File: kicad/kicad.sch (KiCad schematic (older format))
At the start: 46 parts, among them J1 Power, J2 Address In, J3 Counter Reset Value, J4 5V, J5 Mode In, J6 GND, J7 VGA Out, J8 L77HDE15SD1CH4F, J9 Data In, U1 74LS157, U10 SN74LS682N, U11 74LS161, U12 74LS157, U13 74LS157, U14 74LS161, U15 74LS157, U16 74LS157, U17 74LS161, U18 SN74HC32N, U19 74LS161, U2 74LS157, U20 SN74LS04N, U21 AS6C4008-55PCN, U22 SN74LS74AN, U23 AS6C4008-55PCN, U24 SN74LS244N, U25 SN74LS244N, U26 SN74LS244N, U27 SN74LS244N, U3 SN74LS74AN, U4 SN74LS682N, U5 74LS157, U6 74LS157, U7 74LS161, U8 74LS157, U9 74LS157, X1 CXO_DIP8

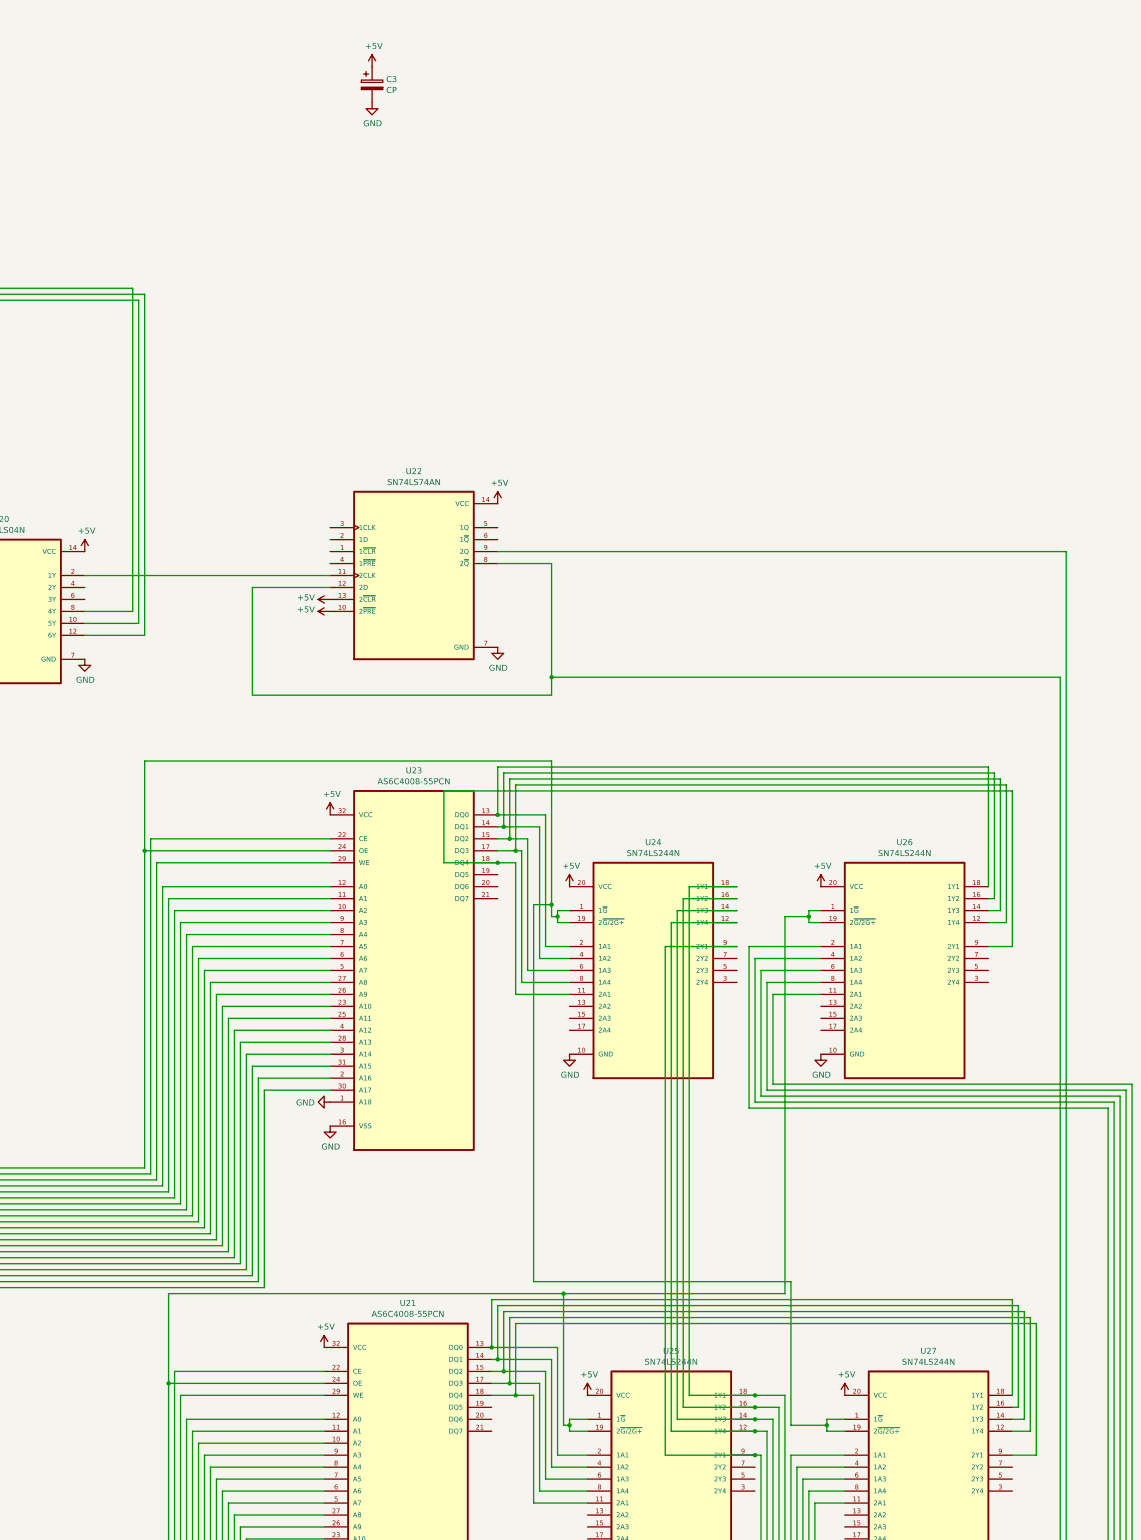
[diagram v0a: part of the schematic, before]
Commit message: Update schematic to account for SRAM enable time.
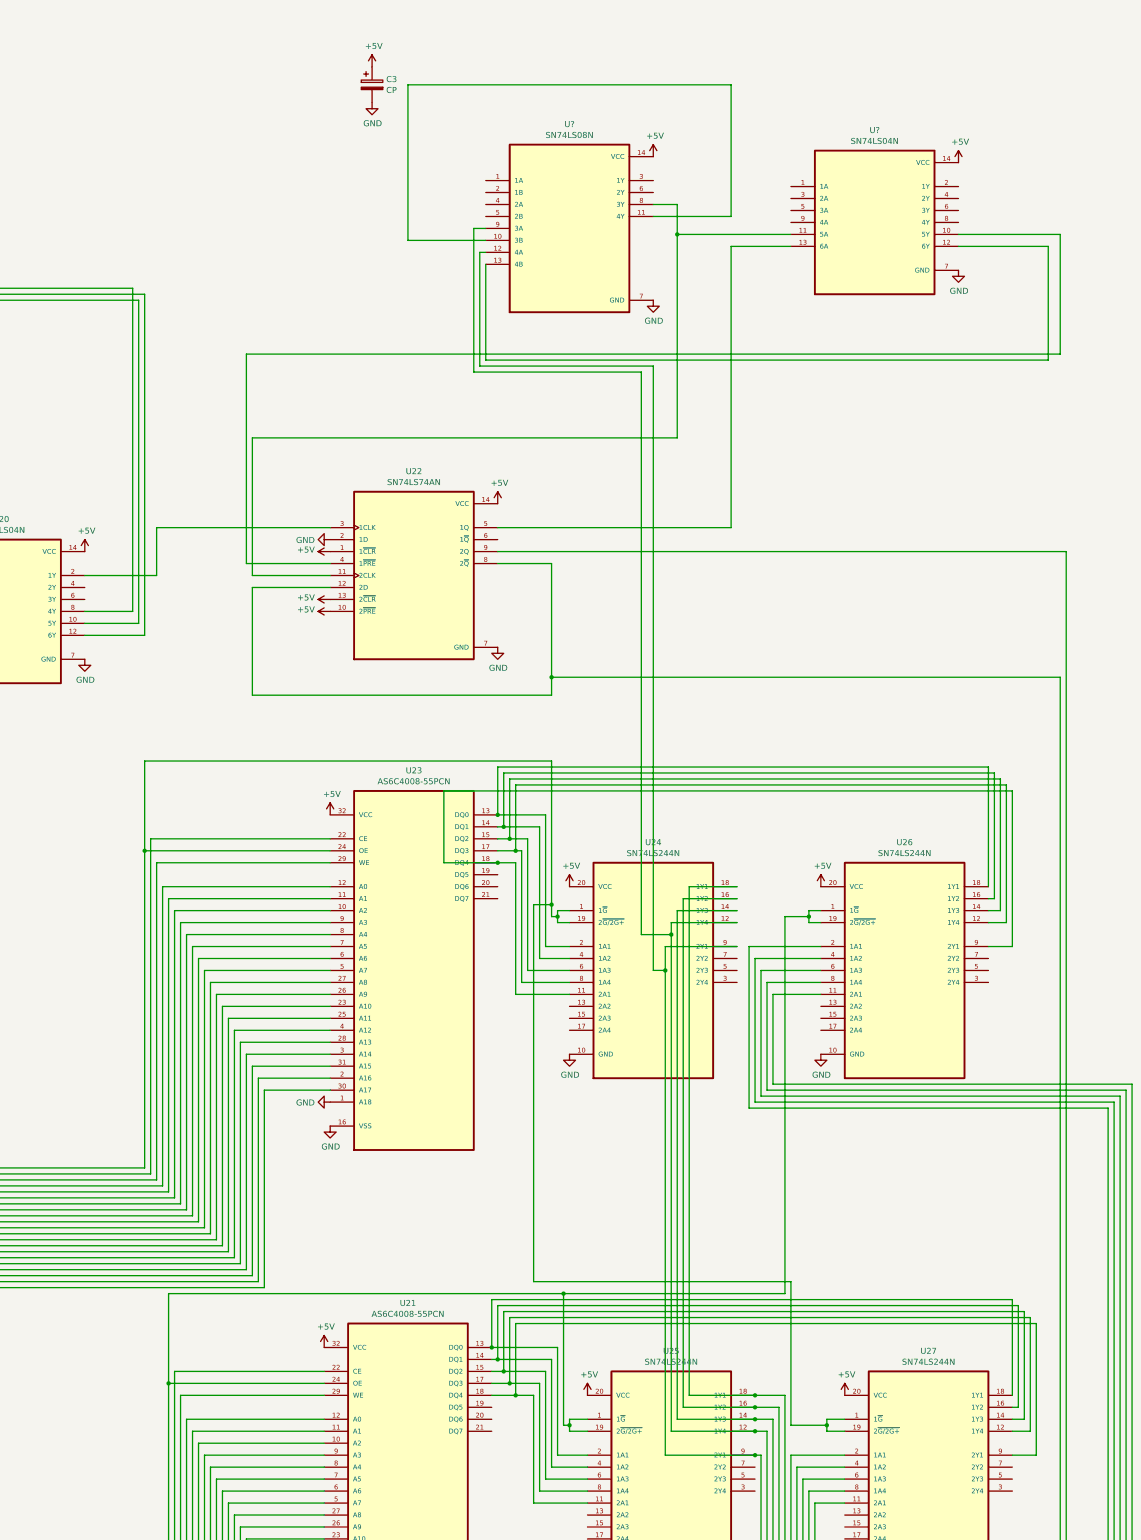
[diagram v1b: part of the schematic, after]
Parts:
- added U?: SN74LS08N, DIP794W45P254L1969H508Q14, symbol SN74LS08N:SN74LS08N
- added U?: SN74LS04N, DIP794W45P254L1969H508Q14, symbol SN74LS04N:SN74LS04N
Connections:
- net +5V: now also U22.1 (1~CLR), U?.14 (VCC), U?.14 (VCC)
- net GND: now also U22.2 (1D), U?.7 (GND), U?.7 (GND)
- net at U20.2 (1Y): now also U22.3 (1CLK); no longer U22.11 (2CLK)
- net at J7.4 (Pin_4), J8.13, U24.12 (1Y4)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: now also U?.9 (3A)
- net at J7.5 (Pin_5), J8.14, U24.9 (2Y1)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: now also U?.12 (4A)
- net at U22.4 (1~PRE): now also U?.10 (5Y)
- net at U22.5 (1Q): now also U?.13 (6A)
- new net: U22.11 (2CLK), U?.11 (5A), U?.8 (3Y)
- new net: U?.10 (3B), U?.11 (4Y)
- new net: U?.12 (6Y), U?.13 (4B)
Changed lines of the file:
@@
 Wire Wire Line
 	10100 9650 10350 9650
-Wire Wire Line
-	16850 6350 18900 6350
 $Comp
 L power:+5V #PWR0118
@@
 	22300 9250 21750 9250
 Wire Wire Line
-	21750 9250 21750 13500
+	21750 9250 21750 9350
 Wire Wire Line
 	21750 13500 22450 13500
@@
 	22300 9450 21700 9450
 Wire Wire Line
-	21700 9450 21700 13700
+	21700 9450 21700 9650
 Wire Wire Line
 	21700 13700 22450 13700
@@
 	1    0    0    -1
 $EndComp
+$Comp
+L SN74LS08N:SN74LS08N U?
+U 1 1 62598C70
+P 20900 3450
+F 0 "U?" H 20900 4320 50  0000 C CNN
+F 1 "SN74LS08N" H 20900 4229 50  0000 C CNN
+F 2 "DIP794W45P254L1969H508Q14" H 20900 3450 50  0001 L BNN
+F 3 "" H 20900 3450 50  0001 L BNN
+	1    20900 3450
+	1    0    0    -1
+$EndComp
+$Comp
+L SN74LS04N:SN74LS04N U?
+U 1 1 6259AFB1
+P 23450 3400
+F 0 "U?" H 23450 4170 50  0000 C CNN
+F 1 "SN74LS04N" H 23450 4079 50  0000 C CNN
+F 2 "DIP794W45P254L1969H508Q14" H 23450 3400 50  0001 L BNN
+F 3 "" H 23450 3400 50  0001 L BNN
+	1    23450 3400
+	1    0    0    -1
+$EndComp
+$Comp
+L power:+5V #PWR?
+U 1 1 625A7E5C
+P 21600 2850
+F 0 "#PWR?" H 21600 2700 50  0001 C CNN
+F 1 "+5V" H 21615 3023 50  0000 C CNN
+F 2 "" H 21600 2850 50  0001 C CNN
+F 3 "" H 21600 2850 50  0001 C CNN
+	1    21600 2850
+	1    0    0    -1
+$EndComp
+$Comp
+L power:+5V #PWR?
+U 1 1 625A8430
+P 24150 2900
+F 0 "#PWR?" H 24150 2750 50  0001 C CNN
+F 1 "+5V" H 24165 3073 50  0000 C CNN
+F 2 "" H 24150 2900 50  0001 C CNN
+F 3 "" H 24150 2900 50  0001 C CNN
+	1    24150 2900
+	1    0    0    -1
+$EndComp
+$Comp
+L power:GND #PWR?
+U 1 1 625A8FC6
+P 21600 4050
+F 0 "#PWR?" H 21600 3800 50  0001 C CNN
+F 1 "GND" H 21605 3877 50  0000 C CNN
+F 2 "" H 21600 4050 50  0001 C CNN
+F 3 "" H 21600 4050 50  0001 C CNN
+	1    21600 4050
+	1    0    0    -1
+$EndComp
+$Comp
+L power:GND #PWR?
+U 1 1 625A953B
+P 24150 3800
+F 0 "#PWR?" H 24150 3550 50  0001 C CNN
+F 1 "GND" H 24155 3627 50  0000 C CNN
+F 2 "" H 24150 3800 50  0001 C CNN
+F 3 "" H 24150 3800 50  0001 C CNN
+	1    24150 3800
+	1    0    0    -1
+$EndComp
+Wire Wire Line
+	16850 6350 17450 6350
+Wire Wire Line
+	17450 6350 17450 5950
+Wire Wire Line
+	17450 5950 18900 5950
+$Comp
+L power:+5V #PWR?
+U 1 1 629D3306
+P 18900 6150
+F 0 "#PWR?" H 18900 6000 50  0001 C CNN
+F 1 "+5V" V 18915 6278 50  0000 L CNN
+F 2 "" H 18900 6150 50  0001 C CNN
+F 3 "" H 18900 6150 50  0001 C CNN
+	1    18900 6150
+	0    -1   -1   0
+$EndComp
+$Comp
+L power:GND #PWR?
+U 1 1 629D39D3
+P 18900 6050
+F 0 "#PWR?" H 18900 5800 50  0001 C CNN
+F 1 "GND" V 18905 5922 50  0000 R CNN
+F 2 "" H 18900 6050 50  0001 C CNN
+F 3 "" H 18900 6050 50  0001 C CNN
+	1    18900 6050
+	0    1    1    0
+$EndComp
+Wire Wire Line
+	18900 6250 18200 6250
+Wire Wire Line
+	18200 6250 18200 4500
+Wire Wire Line
+	18200 4500 25000 4500
+Wire Wire Line
+	25000 4500 25000 3500
+Wire Wire Line
+	25000 3500 24150 3500
+Wire Wire Line
+	20300 5950 22250 5950
+Wire Wire Line
+	22250 5950 22250 3600
+Wire Wire Line
+	22250 3600 22750 3600
+Wire Wire Line
+	20200 3750 20200 4550
+Wire Wire Line
+	20200 4550 24900 4550
+Wire Wire Line
+	24900 4550 24900 3600
+Wire Wire Line
+	24900 3600 24150 3600
+Wire Wire Line
+	21700 9650 21600 9650
+Wire Wire Line
+	21600 9650 21600 4600
+Wire Wire Line
+	21600 4600 20150 4600
+Wire Wire Line
+	20150 4600 20150 3650
+Wire Wire Line
+	20150 3650 20200 3650
+Connection ~ 21700 9650
+Wire Wire Line
+	21700 9650 21700 13700
+Wire Wire Line
+	21600 3350 22250 3350
+Wire Wire Line
+	22250 3350 22250 2250
+Wire Wire Line
+	22250 2250 19550 2250
+Wire Wire Line
+	19550 2250 19550 3550
+Wire Wire Line
+	19550 3550 20200 3550
+Wire Wire Line
+	21750 9350 21500 9350
+Wire Wire Line
+	21500 9350 21500 4650
+Wire Wire Line
+	21500 4650 20100 4650
+Wire Wire Line
+	20100 4650 20100 3450
+Wire Wire Line
+	20100 3450 20200 3450
+Connection ~ 21750 9350
+Wire Wire Line
+	21750 9350 21750 13500
+Wire Wire Line
+	21600 3250 21800 3250
+Wire Wire Line
+	21800 3250 21800 3500
+Wire Wire Line
+	21800 5200 18250 5200
+Wire Wire Line
+	18250 5200 18250 6350
+Wire Wire Line
+	18250 6350 18900 6350
+Wire Wire Line
+	22750 3500 21800 3500
+Connection ~ 21800 3500
+Wire Wire Line
+	21800 3500 21800 5200
 $EndSCHEMATC
